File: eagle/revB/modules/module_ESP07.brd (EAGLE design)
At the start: 24.1 x 32.8 mm, 23 parts

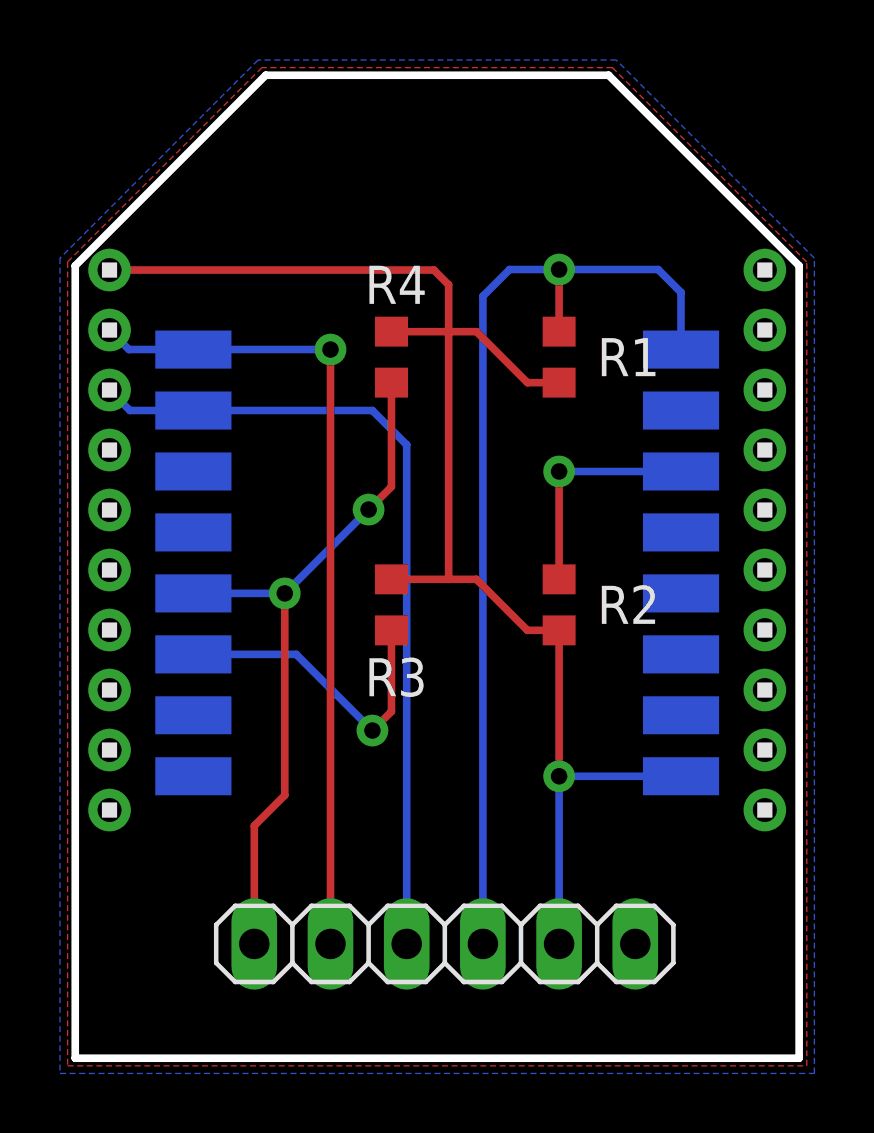
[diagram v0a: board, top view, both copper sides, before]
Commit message: ESP8266 - Added indication LEDs
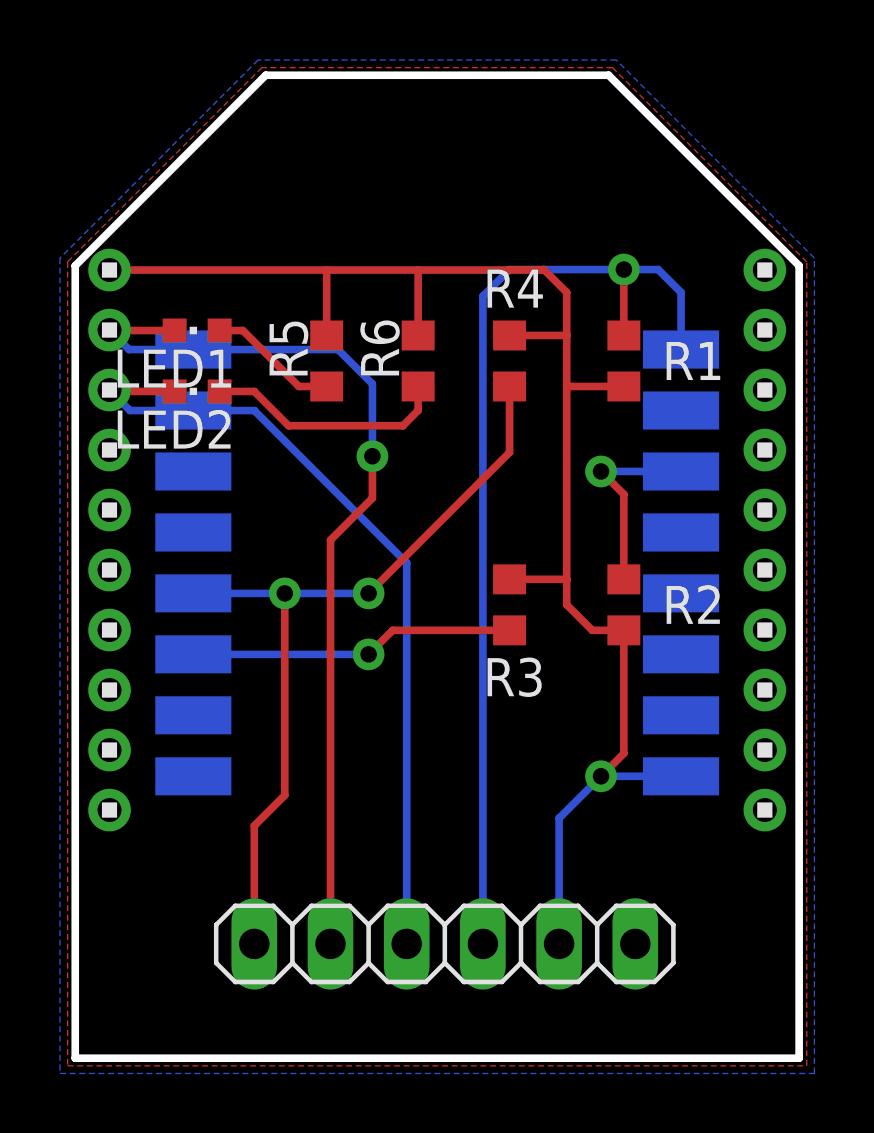
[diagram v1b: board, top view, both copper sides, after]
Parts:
- added LED1, LED2: (no value), led:CHIPLED_0603
- added R5, R6: 1k, rcl:R0603
- moved R4 3.94 mm to (14.6, 23.4)
- moved R3 3.94 mm to (14.6, 15.2)
- moved R1 2.16 mm to (18.4, 23.4)
- moved R2 2.16 mm to (18.4, 15.2)
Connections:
- new net N$3: LED2.A, R6.1
- new net N$4: LED1.A, R5.1
- net UART_RX: now also LED2.C
- net UART_TX: now also LED1.C
- net VCC: now also R5.2, R6.2
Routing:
- net N$3: track 0.00 -> 8.10 mm
- net N$4: track 0.00 -> 4.34 mm
- net VCC: track 48.4 -> 52.3 mm
- net UART_TX: track 27.4 -> 30.9 mm
- net GPIO0: track 23.6 -> 26.8 mm
- net N$2: track 7.66 -> 6.58 mm
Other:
- board text added: "R5"
- board text added: "R6"
- board text added: "Rx"
- board text added: "Tx"
